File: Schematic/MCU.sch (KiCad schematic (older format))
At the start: 6 parts, among them U1 STM32F427VGTx, U2 AH1806-W, U3 FT232RL

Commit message: Add passives
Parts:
- added C? (x8): 100nF, symbol Device:C
- added C? (x2): 4.7uF, symbol Device:C
- added C? (x2): 2.2uF, symbol Device:C
- added D? (x4): LED, symbol Device:LED
- added J?: Micro_SD_Card, symbol Connector:Micro_SD_Card
- added J?: Conn_ARM_JTAG_SWD_10, Connector_PinHeader_1.27mm:PinHeader_2x05_P1.27mm_Vertical_SMD, symbol Connector:Conn_ARM_JTAG_SWD_10
- added R? (x2): 10k, symbol Device:R
- added R? (x4): R, symbol Device:R
- C? (x3): value C -> 100nF
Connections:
- net GND: now also C?.2, C?.2, C?.2, U3.18 (GND), U3.21 (GND), U3.25 (AGND), U3.26 (TEST), U3.7 (GND), C?.1, C?.1, C?.2, C?.2, C?.2, C?.2, C?.2, C?.2, C?.2, C?.2, C?.2, J?.3 (GND), J?.5 (GND), J?.9 (GNDDetect), R?.2, R?.2, R?.2, R?.2
- net VDD: now also U1.6 (VBAT), U3.20 (VCC), U3.4 (VCCIO), C?.1, C?.1, C?.1, C?.1, C?.1, C?.1, C?.1, C?.1, D?.2 (A), J?.1 (VTref), R?.1
- net V1: now reaches U2.1 (VDD)
- net V1: now also C?.1, R?.1
- net at U2.2 (GND): now also C?.2
- net HALL_SENSOR: now reaches U2.3 (OUTPUT)
- net HALL_SENSOR: now also U1.23 (PA0), R?.2
- net RX_TO_STM32: now reaches U3.1 (TXD)
- net RX_TO_STM32: now also U1.69 (PA10)
- net FTDI_PWR_EN: now reaches U3.14 (CBUS3)
- net FTDI_PWR_EN: now also R?.2
- net USB_P: now reaches U3.15 (USBD+)
- net USB_N: now reaches U3.16 (USBD-)
- net at U3.17 (3V3OUT): now also C?.1
- net TX_FROM_STM32: now reaches U3.5 (RXD)
- net TX_FROM_STM32: now also U1.68 (PA9)
- net NRESET: now reaches U1.14 (NRST)
- net NRESET: now also J?.10 (~RESET~)
- net AUDIO_FROM_DAC: now reaches U1.29 (PA4)
- net at U1.49 (VCAP_1): now also C?.2
- net at U1.58 (PD11): now also D?.2 (A)
- net at U1.59 (PD12): now also D?.2 (A)
- net at U1.60 (PD13): now also D?.2 (A)
- net SHUTDOWN_AMP: now reaches U1.65 (PC8)
- net V1_EN: now reaches U1.66 (PC9)
- net at U1.72 (PA13): now also J?.2 (SWDIO/TMS)
- net at U1.73 (VCAP_2): now also C?.2
- net at U1.76 (PA14): now also J?.4 (SWDCLK/TCK)
- net FUEL_SCL: now reaches U1.92 (PB6)
- net FUEL_SDA: now reaches U1.93 (PB7)
- new net: D?.1 (K), R?.1 (x4)
- no-connect marks 0 -> 15
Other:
- moved on the sheet: U2, U3

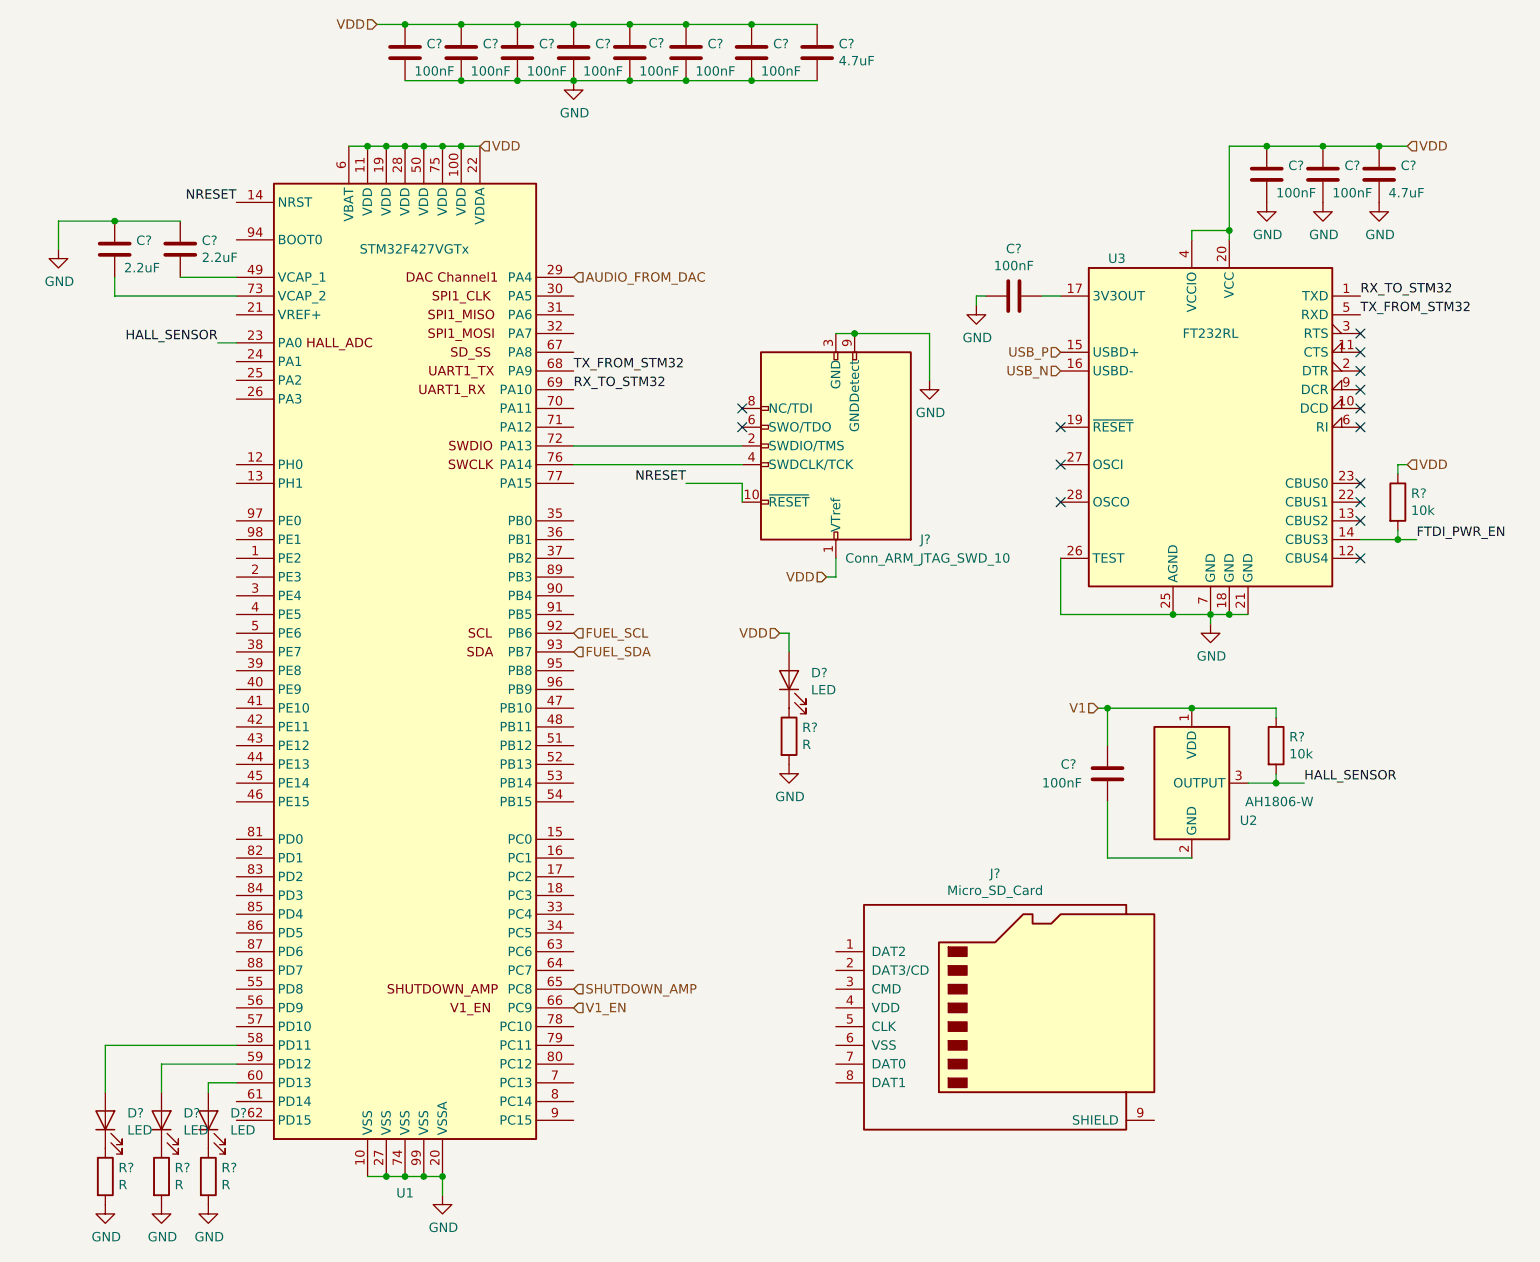
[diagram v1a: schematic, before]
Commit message: Perform annotation start assigning footprints
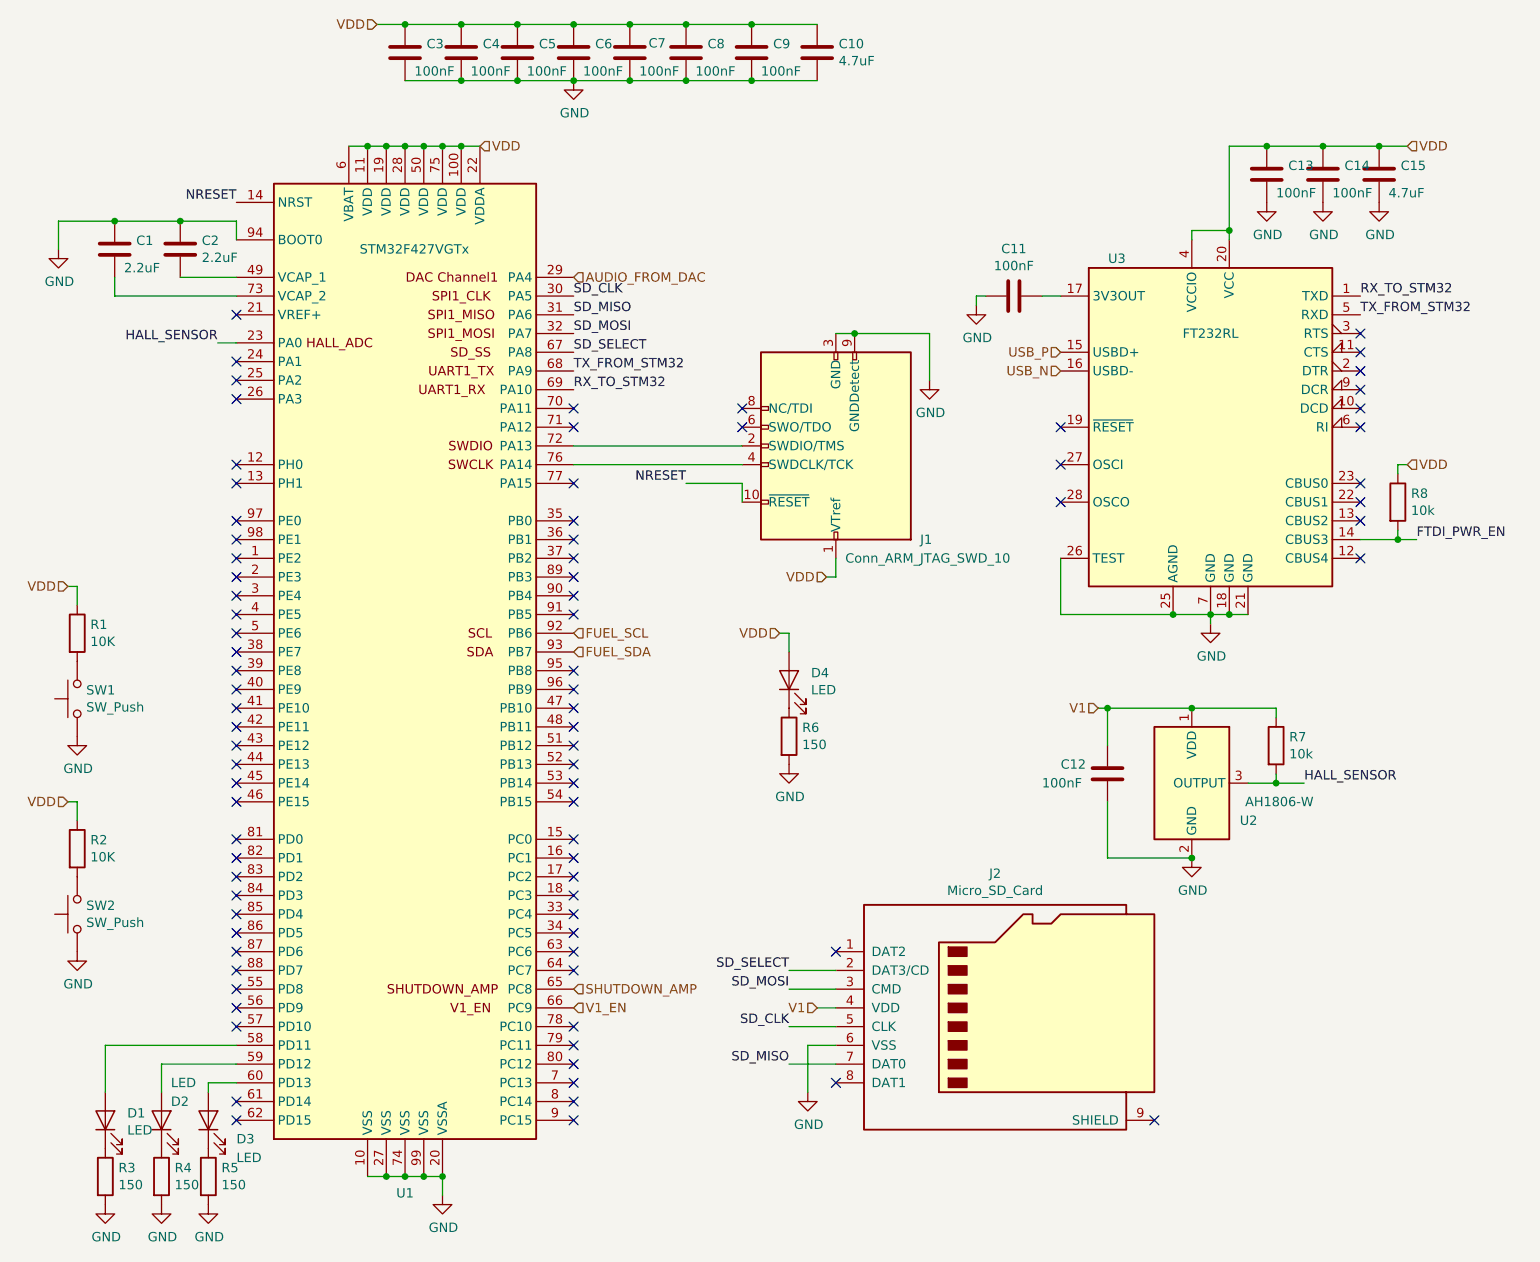
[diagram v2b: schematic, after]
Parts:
- added R1, R2: 10K, Resistor_SMD:R_0603_1608Metric_Pad1.05x0.95mm_HandSolder, symbol Device:R
- added SW1, SW2: SW_Push, symbol Switch:SW_Push
- C11, C12, C13, C14, C3, C4, C5, C6, C7, C8, C9: renamed from C?; footprint (none) -> Capacitor_SMD:C_0603_1608Metric
- D1, D2, D3, D4: renamed from D?; footprint (none) -> Diode_SMD:D_0603_1608Metric_Pad1.05x0.95mm_HandSolder
- R3, R4, R5, R6: renamed from R?; value R -> 150; footprint (none) -> Resistor_SMD:R_0603_1608Metric_Pad1.05x0.95mm_HandSolder
- R7, R8: renamed from R?; footprint (none) -> Resistor_SMD:R_0603_1608Metric_Pad1.05x0.95mm_HandSolder
- gave numbers to parts that had none: 6
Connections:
- net GND: now also C12.2, J2.6 (VSS), U1.94 (BOOT0), U2.2 (GND), SW1.1, SW2.1
- net V1: now also J2.4 (VDD)
- net VDD: now also R1.1, R2.1
- net SD_CLK: now reaches U1.30 (PA5)
- net SD_CLK: now also J2.5 (CLK)
- net SD_MISO: now reaches U1.31 (PA6)
- net SD_MISO: now also J2.7 (DAT0)
- net SD_MOSI: now reaches U1.32 (PA7)
- net SD_MOSI: now also J2.3 (CMD)
- net SD_SELECT: now reaches U1.67 (PA8)
- net SD_SELECT: now also J2.2 (DAT3/CD)
- new net: R1.2, SW1.2
- new net: R2.2, SW2.2
- no-connect marks 15 -> 84

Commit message: Selected components
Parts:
- C1, C10, C15, C2: footprint (none) -> Capacitor_SMD:C_0603_1608Metric_Pad1.05x0.95mm_HandSolder
- C11, C12, C13, C14, C3, C4, C5, C6, C7, C8, C9: footprint Capacitor_SMD:C_0603_1608Metric -> Capacitor_SMD:C_0603_1608Metric_Pad1.05x0.95mm_HandSolder
- J2: footprint (none) -> Connector_Card:microSD_HC_Wuerth_693072010801
- SW1, SW2: footprint (none) -> Button_Switch_SMD:SW_Push_1P1T_NO_6x6mm_H9.5mm
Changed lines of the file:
@@
 EESchema Schematic File Version 4
-LIBS:SoundBoard-cache
-EELAYER 26 0
+EELAYER 30 0
 EELAYER END
 $Descr A4 11693 8268
@@
 F 0 "C3" H 2715 946 50  0000 L CNN
 F 1 "100nF" H 2650 800 50  0000 L CNN
-F 2 "Capacitor_SMD:C_0603_1608Metric" H 2638 750 50  0001 C CNN
+F 2 "Capacitor_SMD:C_0603_1608Metric_Pad1.05x0.95mm_HandSolder" H 2638 750 50  0001 C CNN
 F 3 "~" H 2600 900 50  0001 C CNN
 	1    2600 900
@@
 F 0 "C4" H 3015 946 50  0000 L CNN
 F 1 "100nF" H 2950 800 50  0000 L CNN
-F 2 "Capacitor_SMD:C_0603_1608Metric" H 2938 750 50  0001 C CNN
+F 2 "Capacitor_SMD:C_0603_1608Metric_Pad1.05x0.95mm_HandSolder" H 2938 750 50  0001 C CNN
 F 3 "~" H 2900 900 50  0001 C CNN
 	1    2900 900
@@
 F 0 "C5" H 3315 946 50  0000 L CNN
 F 1 "100nF" H 3250 800 50  0000 L CNN
-F 2 "Capacitor_SMD:C_0603_1608Metric" H 3238 750 50  0001 C CNN
+F 2 "Capacitor_SMD:C_0603_1608Metric_Pad1.05x0.95mm_HandSolder" H 3238 750 50  0001 C CNN
 F 3 "~" H 3200 900 50  0001 C CNN
 	1    3200 900
@@
 F 0 "C12" H 6100 4800 50  0000 L CNN
 F 1 "100nF" H 6000 4700 50  0000 L CNN
-F 2 "Capacitor_SMD:C_0603_1608Metric" H 6388 4600 50  0001 C CNN
+F 2 "Capacitor_SMD:C_0603_1608Metric_Pad1.05x0.95mm_HandSolder" H 6388 4600 50  0001 C CNN
 F 3 "~" H 6350 4750 50  0001 C CNN
 	1    6350 4750
@@
 F 0 "C11" V 5598 2200 50  0000 C CNN
 F 1 "100nF" V 5689 2200 50  0000 C CNN
-F 2 "Capacitor_SMD:C_0603_1608Metric" H 5888 2050 50  0001 C CNN
+F 2 "Capacitor_SMD:C_0603_1608Metric_Pad1.05x0.95mm_HandSolder" H 5888 2050 50  0001 C CNN
 F 3 "~" H 5850 2200 50  0001 C CNN
 	1    5850 2200
@@
 F 0 "C13" H 7315 1596 50  0000 L CNN
 F 1 "100nF" H 7250 1450 50  0000 L CNN
-F 2 "Capacitor_SMD:C_0603_1608Metric" H 7238 1400 50  0001 C CNN
+F 2 "Capacitor_SMD:C_0603_1608Metric_Pad1.05x0.95mm_HandSolder" H 7238 1400 50  0001 C CNN
 F 3 "~" H 7200 1550 50  0001 C CNN
 	1    7200 1550
@@
 F 0 "C15" H 7915 1596 50  0000 L CNN
 F 1 "4.7uF" H 7850 1450 50  0000 L CNN
-F 2 "" H 7838 1400 50  0001 C CNN
+F 2 "Capacitor_SMD:C_0603_1608Metric_Pad1.05x0.95mm_HandSolder" H 7838 1400 50  0001 C CNN
 F 3 "~" H 7800 1550 50  0001 C CNN
 	1    7800 1550
@@
 F 0 "C14" H 7615 1596 50  0000 L CNN
 F 1 "100nF" H 7550 1450 50  0000 L CNN
-F 2 "Capacitor_SMD:C_0603_1608Metric" H 7538 1400 50  0001 C CNN
+F 2 "Capacitor_SMD:C_0603_1608Metric_Pad1.05x0.95mm_HandSolder" H 7538 1400 50  0001 C CNN
 F 3 "~" H 7500 1550 50  0001 C CNN
 	1    7500 1550
@@
 F 0 "C6" H 3615 946 50  0000 L CNN
 F 1 "100nF" H 3550 800 50  0000 L CNN
-F 2 "Capacitor_SMD:C_0603_1608Metric" H 3538 750 50  0001 C CNN
+F 2 "Capacitor_SMD:C_0603_1608Metric_Pad1.05x0.95mm_HandSolder" H 3538 750 50  0001 C CNN
 F 3 "~" H 3500 900 50  0001 C CNN
 	1    3500 900
@@
 F 0 "C7" H 3900 950 50  0000 L CNN
 F 1 "100nF" H 3850 800 50  0000 L CNN
-F 2 "Capacitor_SMD:C_0603_1608Metric" H 3838 750 50  0001 C CNN
+F 2 "Capacitor_SMD:C_0603_1608Metric_Pad1.05x0.95mm_HandSolder" H 3838 750 50  0001 C CNN
 F 3 "~" H 3800 900 50  0001 C CNN
 	1    3800 900
@@
 F 0 "C8" H 4215 946 50  0000 L CNN
 F 1 "100nF" H 4150 800 50  0000 L CNN
-F 2 "Capacitor_SMD:C_0603_1608Metric" H 4138 750 50  0001 C CNN
+F 2 "Capacitor_SMD:C_0603_1608Metric_Pad1.05x0.95mm_HandSolder" H 4138 750 50  0001 C CNN
 F 3 "~" H 4100 900 50  0001 C CNN
 	1    4100 900
@@
 F 0 "C9" H 4565 946 50  0000 L CNN
 F 1 "100nF" H 4500 800 50  0000 L CNN
-F 2 "Capacitor_SMD:C_0603_1608Metric" H 4488 750 50  0001 C CNN
+F 2 "Capacitor_SMD:C_0603_1608Metric_Pad1.05x0.95mm_HandSolder" H 4488 750 50  0001 C CNN
 F 3 "~" H 4450 900 50  0001 C CNN
 	1    4450 900
@@
 F 0 "C2" H 1515 1996 50  0000 L CNN
 F 1 "2.2uF" H 1515 1905 50  0000 L CNN
-F 2 "" H 1438 1800 50  0001 C CNN
+F 2 "Capacitor_SMD:C_0603_1608Metric_Pad1.05x0.95mm_HandSolder" H 1438 1800 50  0001 C CNN
 F 3 "~" H 1400 1950 50  0001 C CNN
 	1    1400 1950
@@
 F 0 "C1" H 1165 1996 50  0000 L CNN
 F 1 "2.2uF" H 1100 1850 50  0000 L CNN
-F 2 "" H 1088 1800 50  0001 C CNN
+F 2 "Capacitor_SMD:C_0603_1608Metric_Pad1.05x0.95mm_HandSolder" H 1088 1800 50  0001 C CNN
 F 3 "~" H 1050 1950 50  0001 C CNN
 	1    1050 1950
@@
 F 0 "C10" H 4915 946 50  0000 L CNN
 F 1 "4.7uF" H 4915 855 50  0000 L CNN
-F 2 "" H 4838 750 50  0001 C CNN
+F 2 "Capacitor_SMD:C_0603_1608Metric_Pad1.05x0.95mm_HandSolder" H 4838 750 50  0001 C CNN
 F 3 "~" H 4800 900 50  0001 C CNN
 	1    4800 900
@@
 F 0 "J2" H 5750 6717 50  0000 C CNN
 F 1 "Micro_SD_Card" H 5750 6626 50  0000 C CNN
-F 2 "" H 6950 6300 50  0001 C CNN
+F 2 "Connector_Card:microSD_HC_Wuerth_693072010801" H 6950 6300 50  0001 C CNN
 F 3 "http://katalog.we-online.de/em/datasheet/693072010801.pdf" H 5800 6000 50  0001 C CNN
 	1    5800 6000
@@
 F 0 "SW1" V 896 4302 50  0000 R CNN
 F 1 "SW_Push" V 805 4302 50  0000 R CNN
-F 2 "" H 850 4550 50  0001 C CNN
+F 2 "Button_Switch_SMD:SW_Push_1P1T_NO_6x6mm_H9.5mm" H 850 4550 50  0001 C CNN
 F 3 "" H 850 4550 50  0001 C CNN
 	1    850  4350
@@
 F 0 "SW2" V 896 5452 50  0000 R CNN
 F 1 "SW_Push" V 805 5452 50  0000 R CNN
-F 2 "" H 850 5700 50  0001 C CNN
+F 2 "Button_Switch_SMD:SW_Push_1P1T_NO_6x6mm_H9.5mm" H 850 5700 50  0001 C CNN
 F 3 "" H 850 5700 50  0001 C CNN
 	1    850  5500

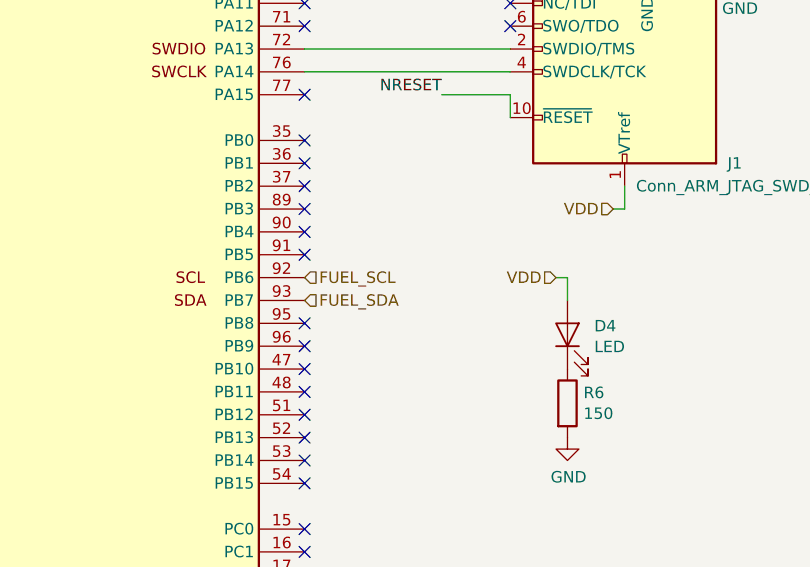
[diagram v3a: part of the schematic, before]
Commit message: Add i2c pullups and start placement
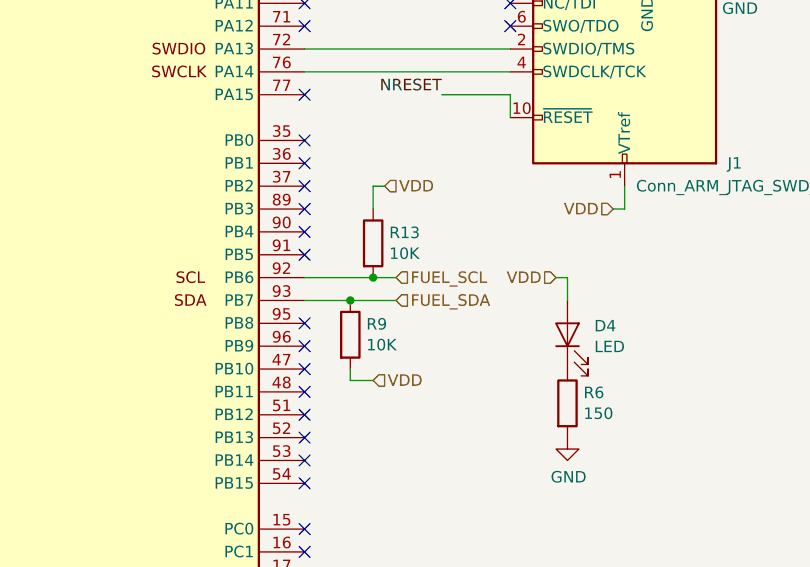
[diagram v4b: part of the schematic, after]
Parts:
- added R13, R9: 10K, Resistor_SMD:R_0603_1608Metric_Pad1.05x0.95mm_HandSolder, symbol Device:R
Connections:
- net FUEL_SCL: now also R13.2
- net FUEL_SDA: now also R9.1
- net VDD: now also R13.1, R9.2
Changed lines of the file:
@@
 	6300 4400 6350 4400
 Connection ~ 6350 4400
-Text HLabel 3500 4100 2    50   Input ~ 0
+Text HLabel 3900 4100 2    50   Input ~ 0
 FUEL_SDA
-Text HLabel 3500 4000 2    50   Input ~ 0
+Text HLabel 3900 4000 2    50   Input ~ 0
 FUEL_SCL
 Text HLabel 3500 6000 2    50   Input ~ 0
@@
 Connection ~ 1400 1800
 NoConn ~ 6600 6600
+$Comp
+L Device:R R13
+U 1 1 5E38C0E0
+P 3800 3850
+F 0 "R13" H 3870 3896 50  0000 L CNN
+F 1 "10K" H 3870 3805 50  0000 L CNN
+F 2 "Resistor_SMD:R_0603_1608Metric_Pad1.05x0.95mm_HandSolder" V 3730 3850 50  0001 C CNN
+F 3 "~" H 3800 3850 50  0001 C CNN
+	1    3800 3850
+	1    0    0    -1
+$EndComp
+$Comp
+L Device:R R9
+U 1 1 5E38C824
+P 3700 4250
+F 0 "R9" H 3770 4296 50  0000 L CNN
+F 1 "10K" H 3770 4205 50  0000 L CNN
+F 2 "Resistor_SMD:R_0603_1608Metric_Pad1.05x0.95mm_HandSolder" V 3630 4250 50  0001 C CNN
+F 3 "~" H 3700 4250 50  0001 C CNN
+	1    3700 4250
+	1    0    0    -1
+$EndComp
+Wire Wire Line
+	3500 4100 3700 4100
+Wire Wire Line
+	3900 4100 3700 4100
+Connection ~ 3700 4100
+Wire Wire Line
+	3500 4000 3800 4000
+Wire Wire Line
+	3800 4000 3900 4000
+Connection ~ 3800 4000
+Text HLabel 3850 3600 2    50   Input ~ 0
+VDD
+Wire Wire Line
+	3850 3600 3800 3600
+Wire Wire Line
+	3800 3600 3800 3700
+Text HLabel 3800 4450 2    50   Input ~ 0
+VDD
+Wire Wire Line
+	3800 4450 3700 4450
+Wire Wire Line
+	3700 4450 3700 4400
 $EndSCHEMATC

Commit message: Preliminary routing
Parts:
- added C25: 100nF, Capacitor_SMD:C_0603_1608Metric_Pad1.05x0.95mm_HandSolder, symbol Device:C
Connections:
- net GND: now also C7.1, C25.2; no longer C7.2
- net VDD: now also C7.2, C25.1; no longer C7.1
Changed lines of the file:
@@
 F 3 "~" H 3800 900 50  0001 C CNN
 	1    3800 900
-	1    0    0    -1
+	1    0    0    1
 $EndComp
 $Comp
@@
 Wire Wire Line
 	3700 4450 3700 4400
+$Comp
+L Device:C C25
+U 1 1 5E44023E
+P 5250 900
+F 0 "C25" H 5365 946 50  0000 L CNN
+F 1 "100nF" H 5300 800 50  0000 L CNN
+F 2 "Capacitor_SMD:C_0603_1608Metric_Pad1.05x0.95mm_HandSolder" H 5288 750 50  0001 C CNN
+F 3 "~" H 5250 900 50  0001 C CNN
+	1    5250 900
+	1    0    0    -1
+$EndComp
+Wire Wire Line
+	5250 750  4800 750
+Connection ~ 4800 750
+Wire Wire Line
+	4800 1050 5250 1050
+Connection ~ 4800 1050
 $EndSCHEMATC
